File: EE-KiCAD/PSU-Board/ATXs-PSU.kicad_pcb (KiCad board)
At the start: 2 copper layers, 80 x 80 mm, 3 parts, among them J101 Conn_02x28_Odd_Even, J104 Conn_02x25_Row_Letter_First, J105 Conn_02x25_Row_Letter_First

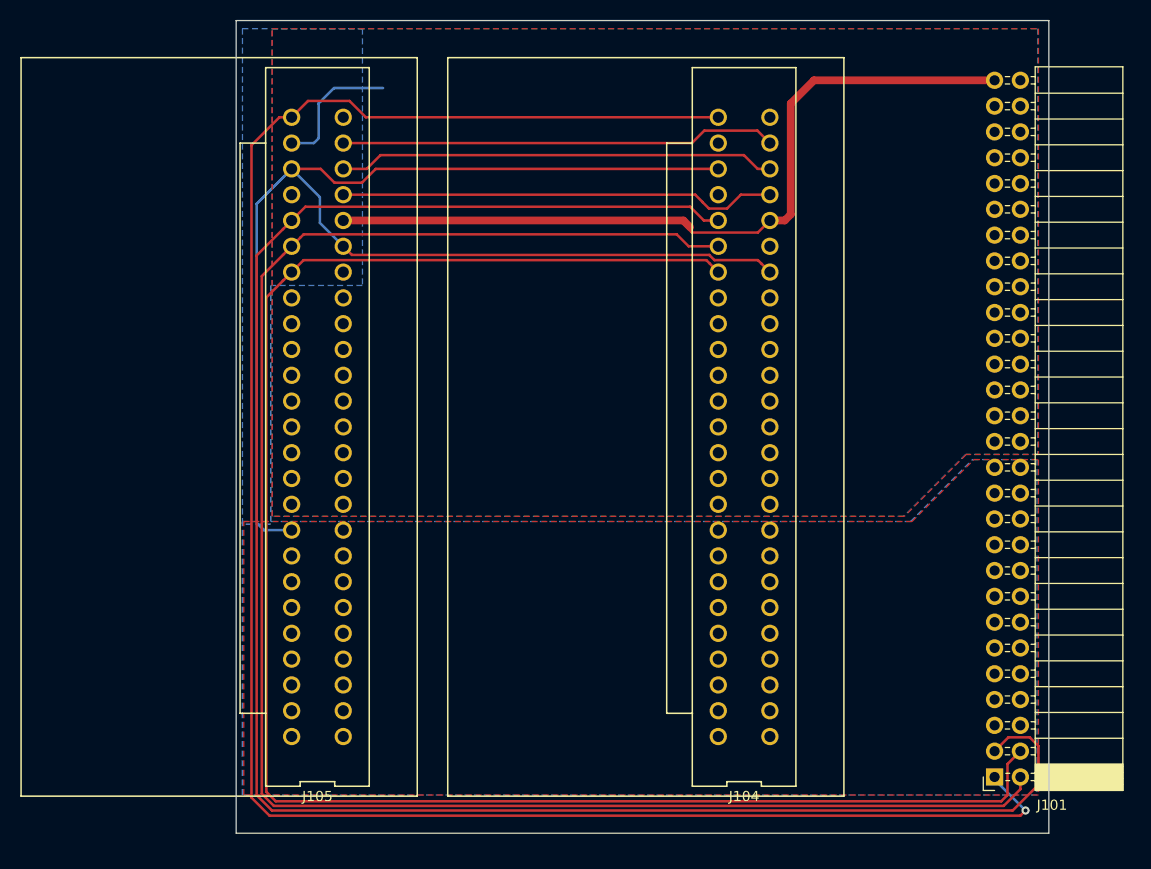
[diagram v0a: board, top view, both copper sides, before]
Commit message: Fitted PSUs into enclosure.  Aligned PSU PCB.
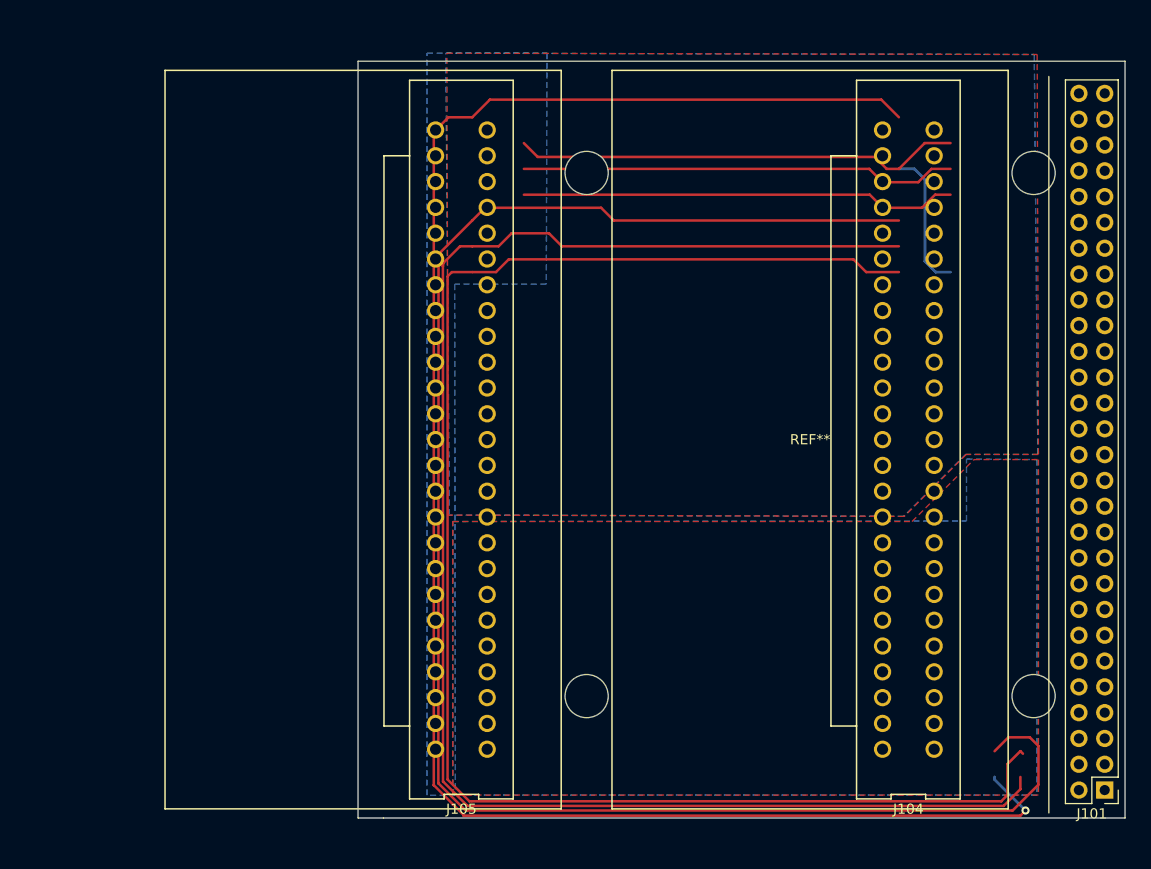
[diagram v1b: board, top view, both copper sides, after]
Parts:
- added REF**: ATXs-PSU-MountHoles, ATXs:ATXs-PSU-MountHoles, F.Cu at (166.5, 90.8)
- J101: footprint Connector_PinSocket_2.54mm:PinSocket_2x28_P2.54mm_Horizontal -> Connector_PinHeader_2.54mm:PinHeader_2x28_P2.54mm_Vertical
- moved J104 16.2 mm to (176.2, 91.2)
- moved J105 14.2 mm to (132.2, 91.2)
- moved J101 10.9 mm to (195.5, 125.8)
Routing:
- net GND: track 178.9 -> 57.1 mm
- net Vstby: track 111.6 -> 0.00 mm
- net /CRPS_PSU/CR_BUS: track 43.1 -> 0.00 mm
- net /CRPS_PSU/CurrentShare: track 43.1 -> 0.00 mm
- net /CRPS_PSU/SMBAlert: track 0.00 -> 43.1 mm
- net Vmain: track 13.3 -> 44.1 mm
- net PSON: track 188.8 -> 170.1 mm
- net PWOK: track 194.4 -> 176.5 mm
- net SCL: track 175.1 -> 157.6 mm
- net SDA: track 174.0 -> 156.6 mm
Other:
- board size 80 x 80 mm -> 75.5 x 74.5 mm

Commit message: add tabs on PCBs to set where they are in the box.  Box adjustments.
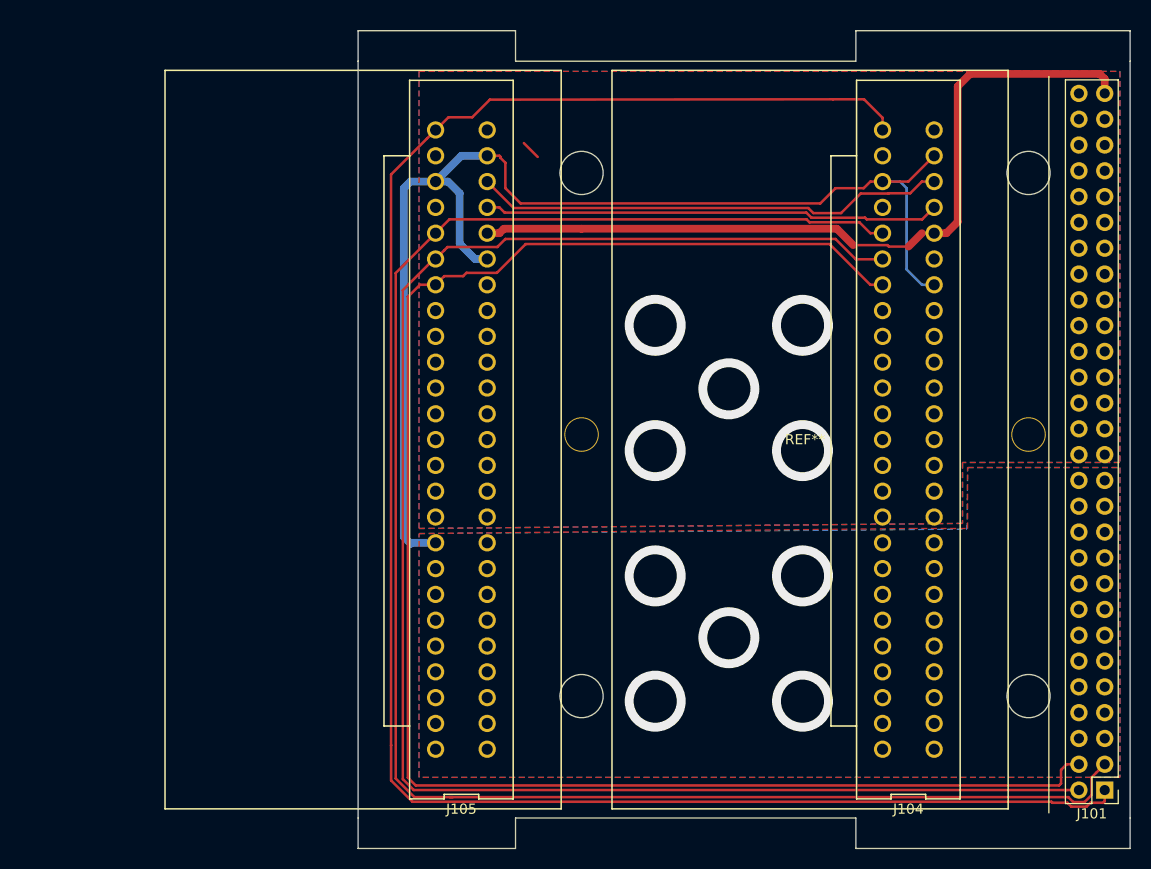
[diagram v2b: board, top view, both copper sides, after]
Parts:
- moved REF** 0.50 mm to (166.0, 90.8)
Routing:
- net Vstby: track 0.00 -> 78.8 mm
- net GND: track 57.1 -> 122.1 mm, vias 0 -> 5
- net /CRPS_PSU/CurrentShare: track 0.00 -> 46.6 mm
- net /CRPS_PSU/CR_BUS: track 0.00 -> 45.0 mm
- net /CRPS_PSU/SMBAlert: track 43.1 -> 0.00 mm
- net Vmain: track 44.1 -> 1.93 mm, vias 0 -> 5
- net PWOK: track 176.5 -> 185.9 mm, vias 1 -> 0
- net SDA: track 156.6 -> 165.9 mm
- net SCL: track 157.6 -> 165.5 mm
- net PSON: track 170.1 -> 174.1 mm
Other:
- board size 75.5 x 74.5 mm -> 76 x 80.5 mm
